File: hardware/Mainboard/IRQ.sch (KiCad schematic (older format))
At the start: 6 parts, among them IC11 74HC148, SW4 NMI

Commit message: Misc: 	- Update README 	- Add 74HC138 datasheet 	- Update board image 	- Add layout for website tutorial
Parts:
- removed R1: 10k, Resistor_THT:R_Axial_DIN0207_L6.3mm_D2.5mm_P7.62mm_Horizontal, symbol Device:R
- added R13: 1k, Resistor_THT:R_Axial_DIN0207_L6.3mm_D2.5mm_P7.62mm_Horizontal, symbol Device:R
- renumbered C17 to C9, IC11 to IC9, R9 to R6, RN3 to RN2, SW4 to SW5
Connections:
- net ~NMI: now also R13.1; no longer SW5.2
- new net: R13.2, SW5.2
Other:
- note added: "NOTE: The W65C22N does need external pull up resistors for the IRQB line, \nbecause of the open collector IRQ output."
- note removed: "NOTE: The W65C22N does need some external pull up resistors for the IRQB line, \nbecause of the Open Collector IRQ output."
- moved on the sheet: C9, R6

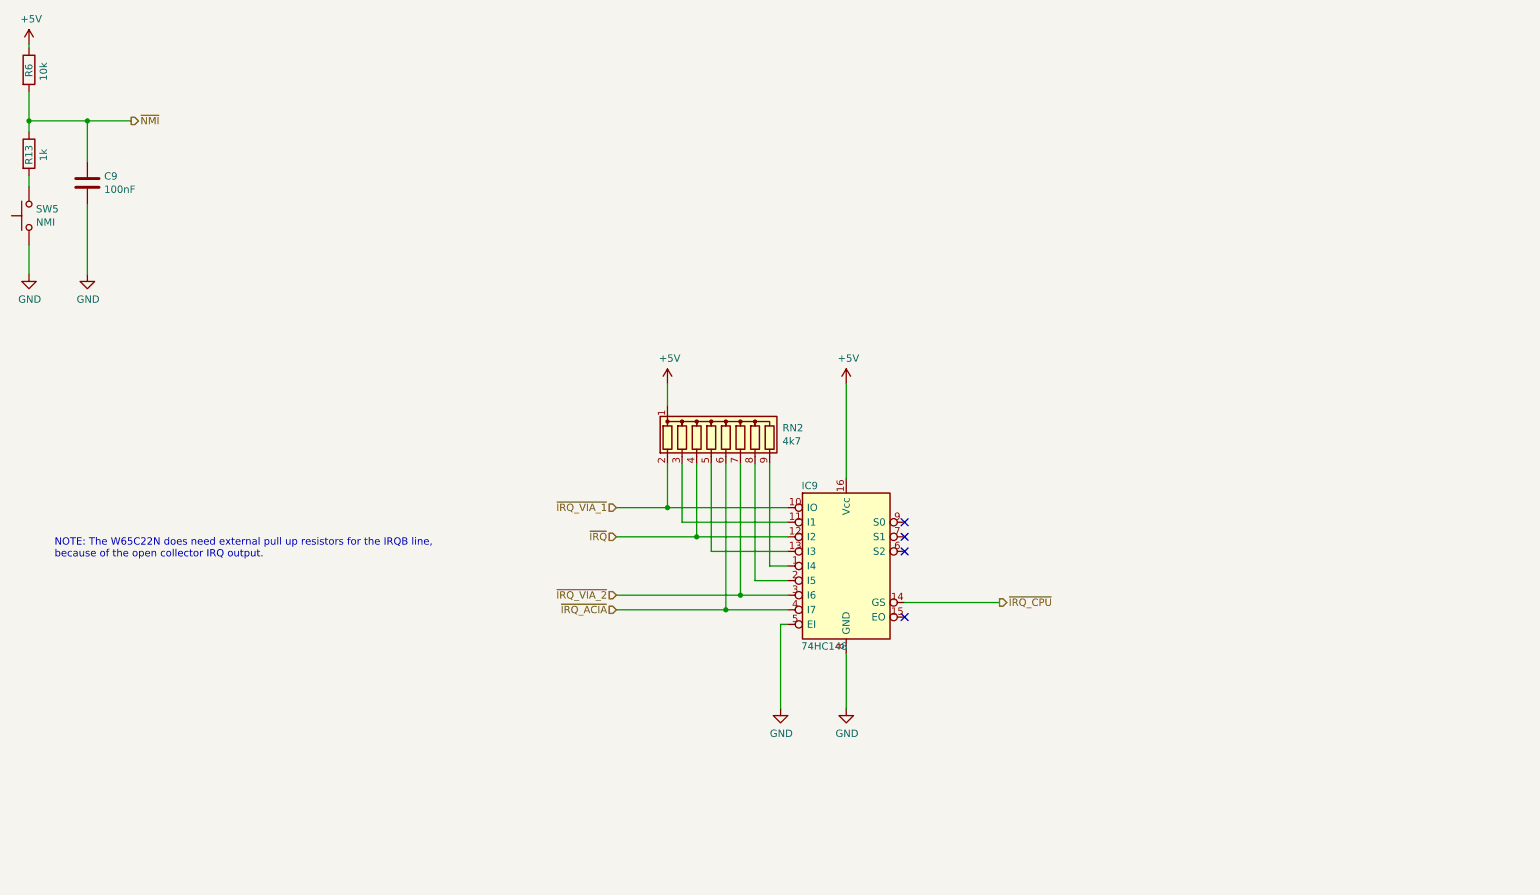
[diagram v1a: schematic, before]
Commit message: Hardware: 	- Add pull up resistor for PB
Documentation:
	- Add more datasheets
	- Update documentation

Misc:
	- Rename CHANGELOG
	- Remove old files

Signed-off-by: Daniel Kampert <DanielKampert@kampis-elektroecke.de>
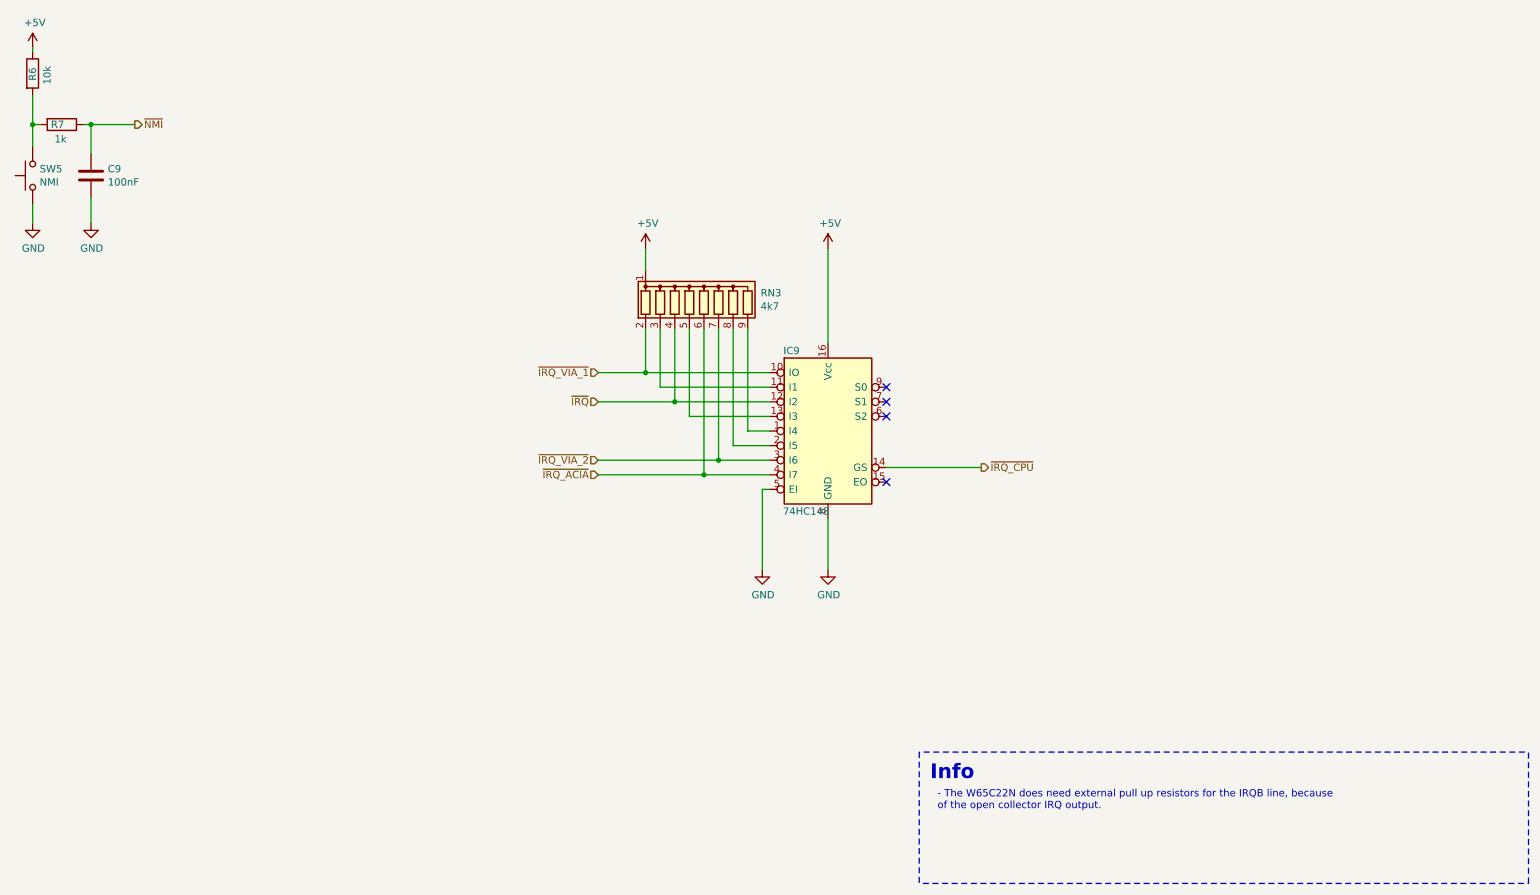
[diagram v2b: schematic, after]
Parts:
- C9: Distributor (none) -> Mouser; Order Number (none) -> 810-FA18X8R1H104KRU6
- IC9: Distributor (none) -> Mouser; Order Number (none) -> 595-SN74HC148N
- R6: Distributor (none) -> Mouser; Order Number (none) -> 603-MFP-25BRD52-10K
- R7: renamed from R13; Distributor (none) -> Mouser; Order Number (none) -> 603-MFP-25BRD52-1K
- RN3: renamed from RN2; Distributor (none) -> Mouser; Order Number (none) -> 652-4609M-1LF-4.7K
- SW5: Distributor (none) -> Mouser; Order Number (none) -> 506-2-1825910-7
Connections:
- net ~NMI: no longer R6.2
- net at R7.2, SW5.2: now also R6.2
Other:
- note added: "- The W65C22N does need external pull up resistors for the IRQB line, because \nof the open collector IRQ output."
- note added: "Info"
- note removed: "NOTE: The W65C22N does need external pull up resistors for the IRQB line, \nbecause of the open collector IRQ output."
- moved on the sheet: C9, IC9, R6, R7, RN3, SW5
